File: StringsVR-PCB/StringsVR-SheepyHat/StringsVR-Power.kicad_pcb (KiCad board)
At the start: 2 copper layers, 164.4 x 85.8 mm, 15 parts, among them J1 Pi4 Pins, SW1 ON/OFF

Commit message: added footprints, new pcb
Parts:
- removed SW1: ON/OFF, Button_Switch_THT:SW_Slide_SPDT_Angled_CK_OS102011MA1Q
- added D1: LED_RABG, LED_THT:LED_D5.0mm-4_RGB, F.Cu at (49.8, 62.3)
- added H1: MountingHole, MountingHole:MountingHole_2.7mm, F.Cu at (44.5, 62.0)
- added H2: MountingHole, MountingHole:MountingHole_2.7mm, F.Cu at (44.5, 69.0)
- added H3: MountingHole, MountingHole:MountingHole_2.7mm, F.Cu at (44.5, 75.9)
- added H4: MountingHole, MountingHole:MountingHole_2.7mm, F.Cu at (44.5, 82.9)
- added J1: MPU6050, Strings_Custom_Symbols:MPU6050, F.Cu at (266.8, 26.6)
- added J2: Conn_02x20_Odd_Even, Strings_Custom_Symbols:Pin_Header_Straight_2x20_Pitch2.54mm, F.Cu at (99.6, 61.3)
- added R1: 220, Resistor_SMD:R_0603_1608Metric, F.Cu at (50.0, 67.4)
- added R2: 220, Resistor_SMD:R_0603_1608Metric, F.Cu at (50.0, 69.9)
- added R3: 220, Resistor_SMD:R_0603_1608Metric, F.Cu at (50.0, 72.4)
- added SW2: SRB22A2BBBNN, Strings_Custom_Symbols:SW_SRB22A2BBBNN_ZFE, F.Cu at (167.0, 69.8)
- added U1: ~, Strings_Custom_Symbols:nRF24L01, F.Cu at (29.2, 112.4)
- added U2: ~, Strings_Custom_Symbols:Pro Micro, F.Cu at (147.1, 111.3)
- added U3: ~, Strings_Custom_Symbols:nRF24L01, F.Cu at (41.6, 135.4)
- moved H1 108.7 mm to (232.4, 139.7)
- moved U8 102.8 mm to (182.0, 137.2), turned to 90 degrees
- moved U7 82.7 mm to (73.7, 137.4), turned to 90 degrees
- moved H3 65.4 mm to (266.7, 91.4)
- moved H1 63.1 mm to (264.2, 108.0)
- moved H1 53.0 mm to (236.2, 124.5)
- moved H1 50.8 mm to (166.4, 25.4)
- moved H1 49.5 mm to (119.4, 24.1)
- moved H3 48.6 mm to (39.4, 106.7)
- moved H3 41.8 mm to (43.2, 45.7)
- moved U5 35.4 mm to (171.4, 86.4)
- moved U6 14.5 mm to (107.6, 115.6)
- renumbered U1 to U4, U4 to U6, U2 to U7, U3 to U8
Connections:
- net 3.3V2 renamed Net-(SW2-Pad2)
- U4 pad 3: 3.3V -> Net-(U4-OUT+)
- U5 pad 5: Net-(J1-Pin_1) -> GND
- U5 pad 6: Net-(J1-Pin_2) -> Net-(U5-VOUT)
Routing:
- net /B+: track 189.1 -> 0.00 mm, vias 1 -> 0
- net /B-: track 98.9 -> 0.00 mm
- net 3.3V: track 62.8 -> 0.00 mm
- net Net-(SW2-Pad2): track 31.2 -> 0.00 mm, vias 1 -> 0
- net Net-(J1-Pin_2): track 23.9 -> 0.00 mm, vias 1 -> 0
- net Net-(J1-Pin_1): track 21.8 -> 0.00 mm
- net GND: track 18.6 -> 0.14 mm
- net Net-(U5-VOUT): vias 0 -> 1
- net +3.3V: vias 0 -> 1
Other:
- board size 164.4 x 85.8 mm -> 209.1 x 93 mm

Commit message: progress on new pcb
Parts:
- removed H1 (x5), H3 (x3): MountingHole, MountingHole:MountingHole_2.5mm
- removed H1, H2, H3, H4: MountingHole, MountingHole:MountingHole_2.7mm
- removed the J1 at (219.9, 85.7)
- added REF**: StringsVRPCB, Strings_Custom_Symbols:StringsVRPCB, F.Cu at (86.5, 54.8)
- moved J1 118.5 mm to (177.5, 104.6)
- moved U1 96.1 mm to (110.6, 61.4)
- moved D1 90.3 mm to (140.0, 57.3)
- moved U3 90.3 mm to (111.1, 77.8)
- moved R3 87.5 mm to (136.6, 59.5), turned to 90 degrees
- moved R2 84.7 mm to (134.0, 59.5), turned to 90 degrees
- moved R1 81.9 mm to (131.5, 59.5), turned to 90 degrees
- moved U4 75.9 mm to (129.5, 120.8), turned to 90 degrees
- moved U6 3.38 mm to (107.6, 112.2)
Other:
- board size 209.1 x 93 mm -> 145 x 85 mm

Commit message: progress on new pcb
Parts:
- moved U2 149.8 mm to (287.7, 59.7)
- moved U7 106.8 mm to (179.8, 125.9), turned to 180 degrees
- moved U5 85.4 mm to (88.0, 104.8), turned to 180 degrees
- moved J1 81.6 mm to (225.0, 38.3), turned to 90 degrees
- moved U6 72.6 mm to (179.8, 105.0), turned to 180 degrees
- moved R1 66.0 mm to (188.5, 26.1)
- moved R2 66.0 mm to (191.0, 26.1)
- moved R3 66.0 mm to (193.6, 26.1)
- moved U4 64.2 mm to (87.5, 72.3), turned to 0 degrees
- moved SW2 62.5 mm to (104.5, 68.8), turned to -90 degrees
- moved U1 56.5 mm to (156.1, 27.8)
- moved U3 50.4 mm to (120.6, 28.4)
- moved D1 45.8 mm to (173.7, 26.3)
- moved J2 9.80 mm to (108.5, 57.0)
- moved U8 9.02 mm to (179.8, 146.0), turned to 180 degrees
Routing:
- net /B+: track 0.00 -> 182.2 mm
- net /B-: track 0.00 -> 51.1 mm
- net (no net): track 0.00 -> 1.60 mm
- net GND: track 0.14 -> 0.00 mm, vias 1 -> 0
- net Net-(U5-VOUT): vias 1 -> 0

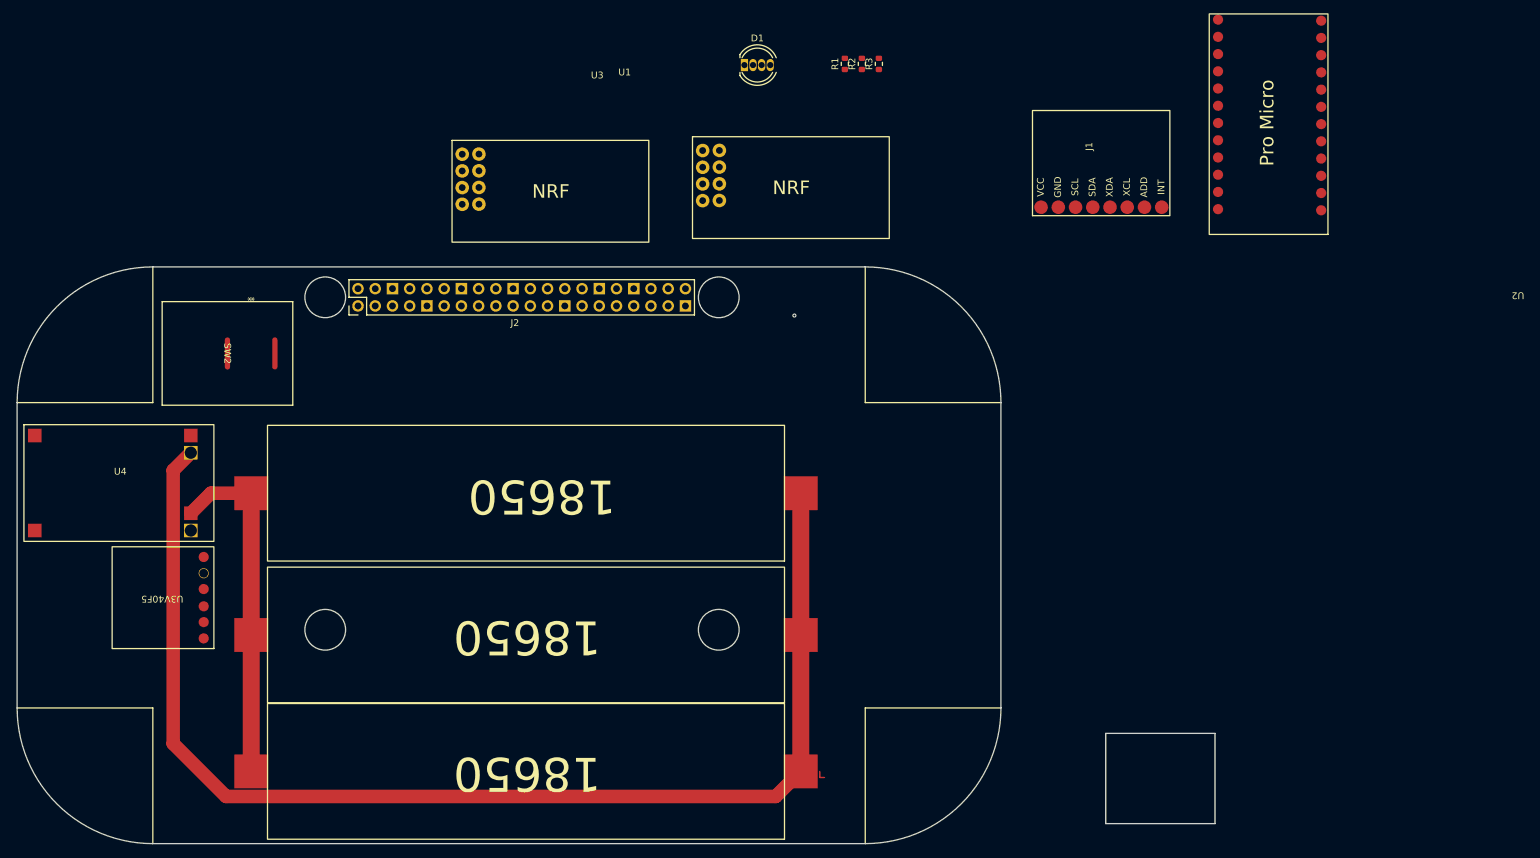
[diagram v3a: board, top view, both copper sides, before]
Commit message: updated pcb design, new footprints, updated schem a lil
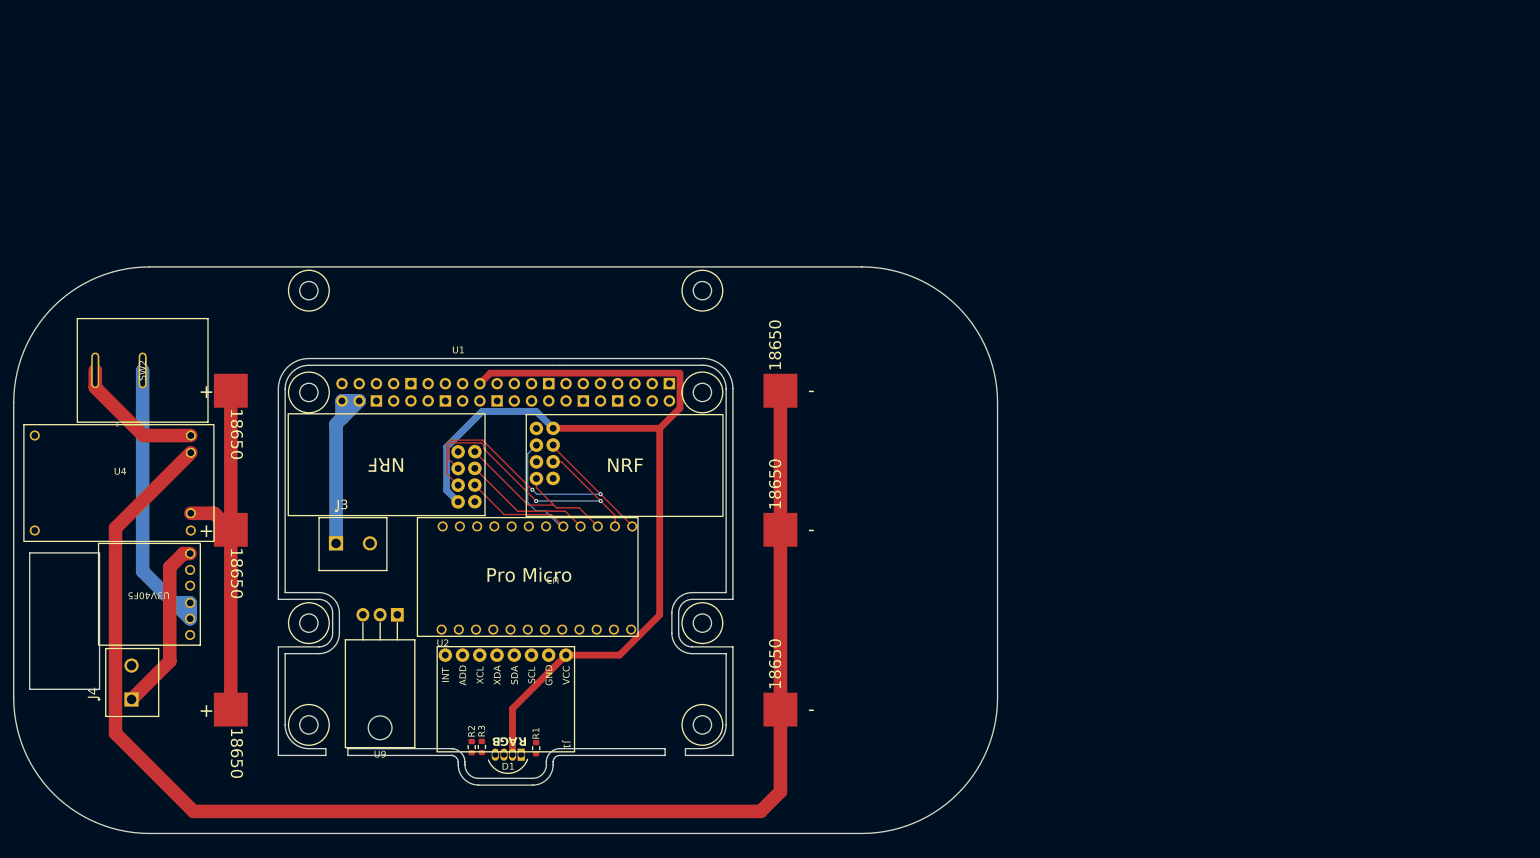
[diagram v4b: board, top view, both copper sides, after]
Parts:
- added J3: Screw_Terminal_01x02, Strings_Custom_Symbols:CUI_TB003-500-P02BE, F.Cu at (113.5, 96.8)
- added J4: Screw_Terminal_01x02, Strings_Custom_Symbols:CUI_TB003-500-P02BE, F.Cu at (83.4, 119.8)
- added U9: LM317_TO-220, Package_TO_SOT_THT:TO-220-3_Horizontal_TabDown, F.Cu at (122.6, 107.3)
- J2: moved to B.Cu
- U6, U7, U8: footprint 18650:18650PCB -> Strings_Custom_Symbols:18650SMD
- moved U2 188.0 mm to (117.0, 138.5), turned to 90 degrees
- moved R3 116.4 mm to (135.0, 126.8)
- moved R2 116.0 mm to (133.5, 126.8)
- moved J1 113.6 mm to (138.6, 112.0), turned to -90 degrees
- moved R1 110.6 mm to (143.0, 127.0)
- moved D1 107.2 mm to (138.9, 127.7), turned to 180 degrees
- moved U3 77.4 mm to (145.5, 101.7), turned to 180 degrees
- moved REF** 68.6 mm to (138.5, 99.5)
- moved U1 47.7 mm to (131.6, 68.8)
- moved SW2 26.6 mm to (78.1, 71.3), turned to 90 degrees
- moved J2 21.1 mm to (106.0, 78.0), turned to -90 degrees
- moved U7 15.8 mm to (176.8, 110.4)
- moved U6 15.4 mm to (176.8, 89.9)
- moved U8 9.58 mm to (176.8, 136.9)
- moved U5 2.06 mm to (86.0, 104.3)
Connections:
- J2 pad 2: unconnected-(J2-Pin_2-Pad2) -> 5V regulated
- J2 pad 4: Net-(J2-Pin_4) -> 5V regulated
- U2 pad 16: Net-(U2-VCC) -> 5V regulated
- U5 pad 6: Net-(U5-VOUT) -> 5V regulated
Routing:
- net +3.3V: track 0.00 -> 144.6 mm, vias 1 -> 0
- net 5V regulated: track 0.00 -> 53.1 mm
- net CSN: track 0.00 -> 49.8 mm, vias 0 -> 2
- net MOSI: track 0.00 -> 44.3 mm, vias 0 -> 2
- net Net-(SW2-Pad2): track 0.00 -> 44.2 mm
- net CE: track 0.00 -> 31.3 mm
- net MISO: track 0.00 -> 27.6 mm
- net /B+: track 182.2 -> 209.0 mm
- net Net-(U4-OUT+): track 0.00 -> 19.5 mm
- net SCK: track 0.00 -> 19.1 mm
- net /B-: track 51.1 -> 53.9 mm
- net (no net): track 1.60 -> 0.00 mm
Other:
- board size 145 x 85 mm -> 145 x 83.5 mm
